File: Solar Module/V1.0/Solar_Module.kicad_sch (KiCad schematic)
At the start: 18 parts, among them J1 B2B-PH-K-S, U1 MT3608, U2 TP4057

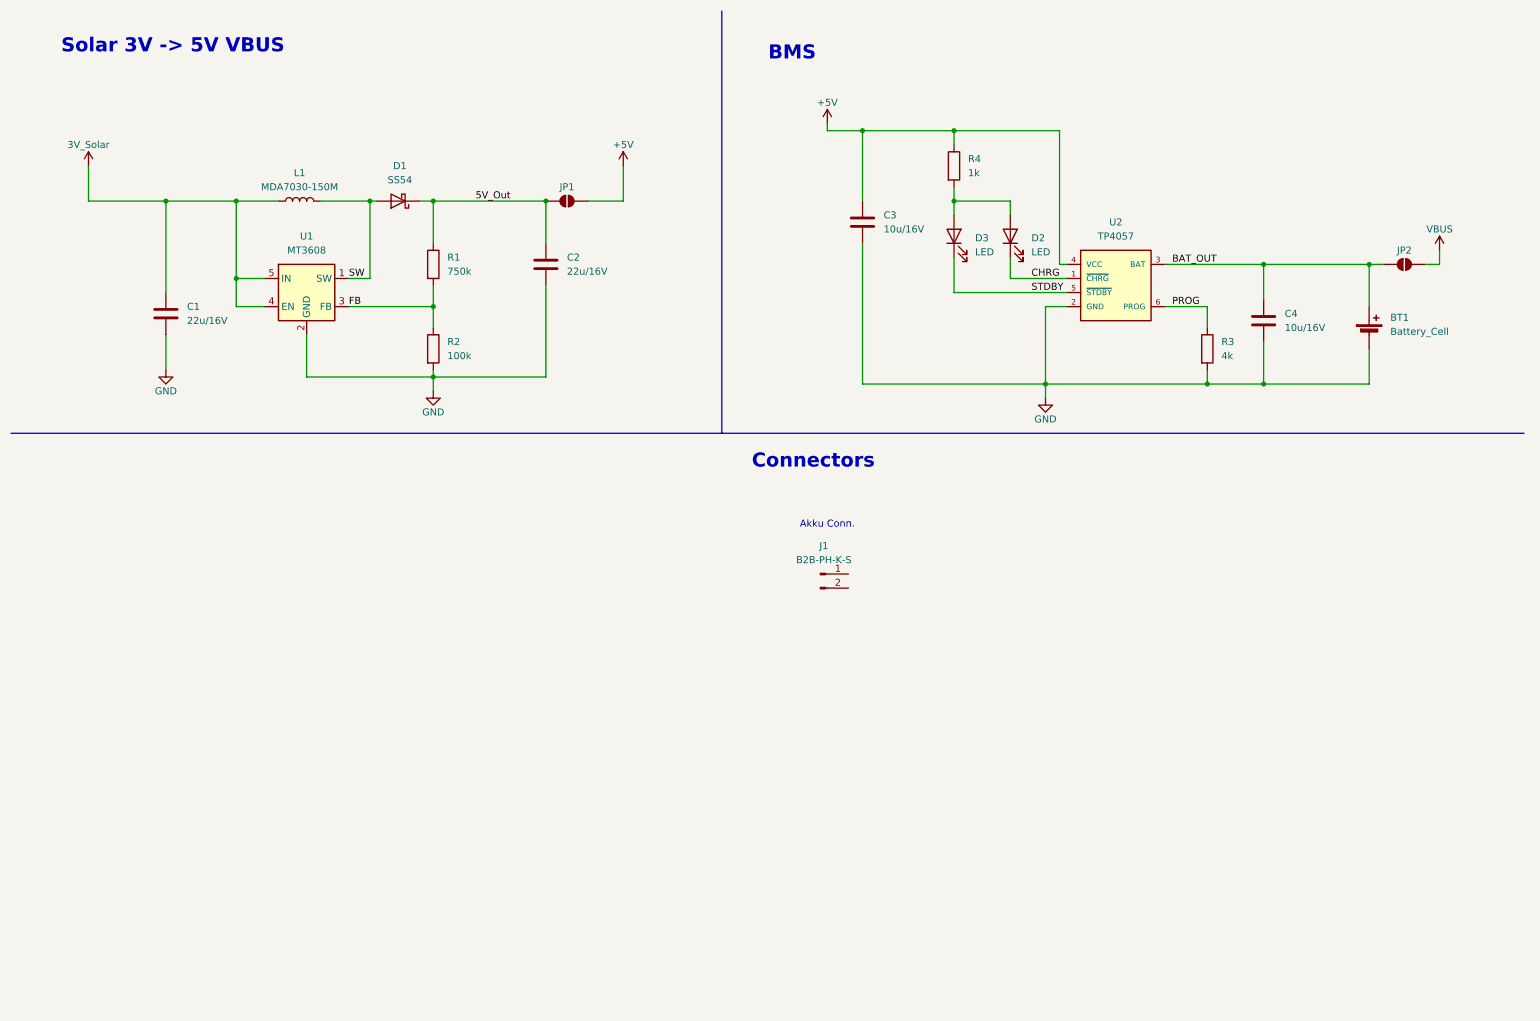
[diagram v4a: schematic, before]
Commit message: Added USB-C connector to schematic.
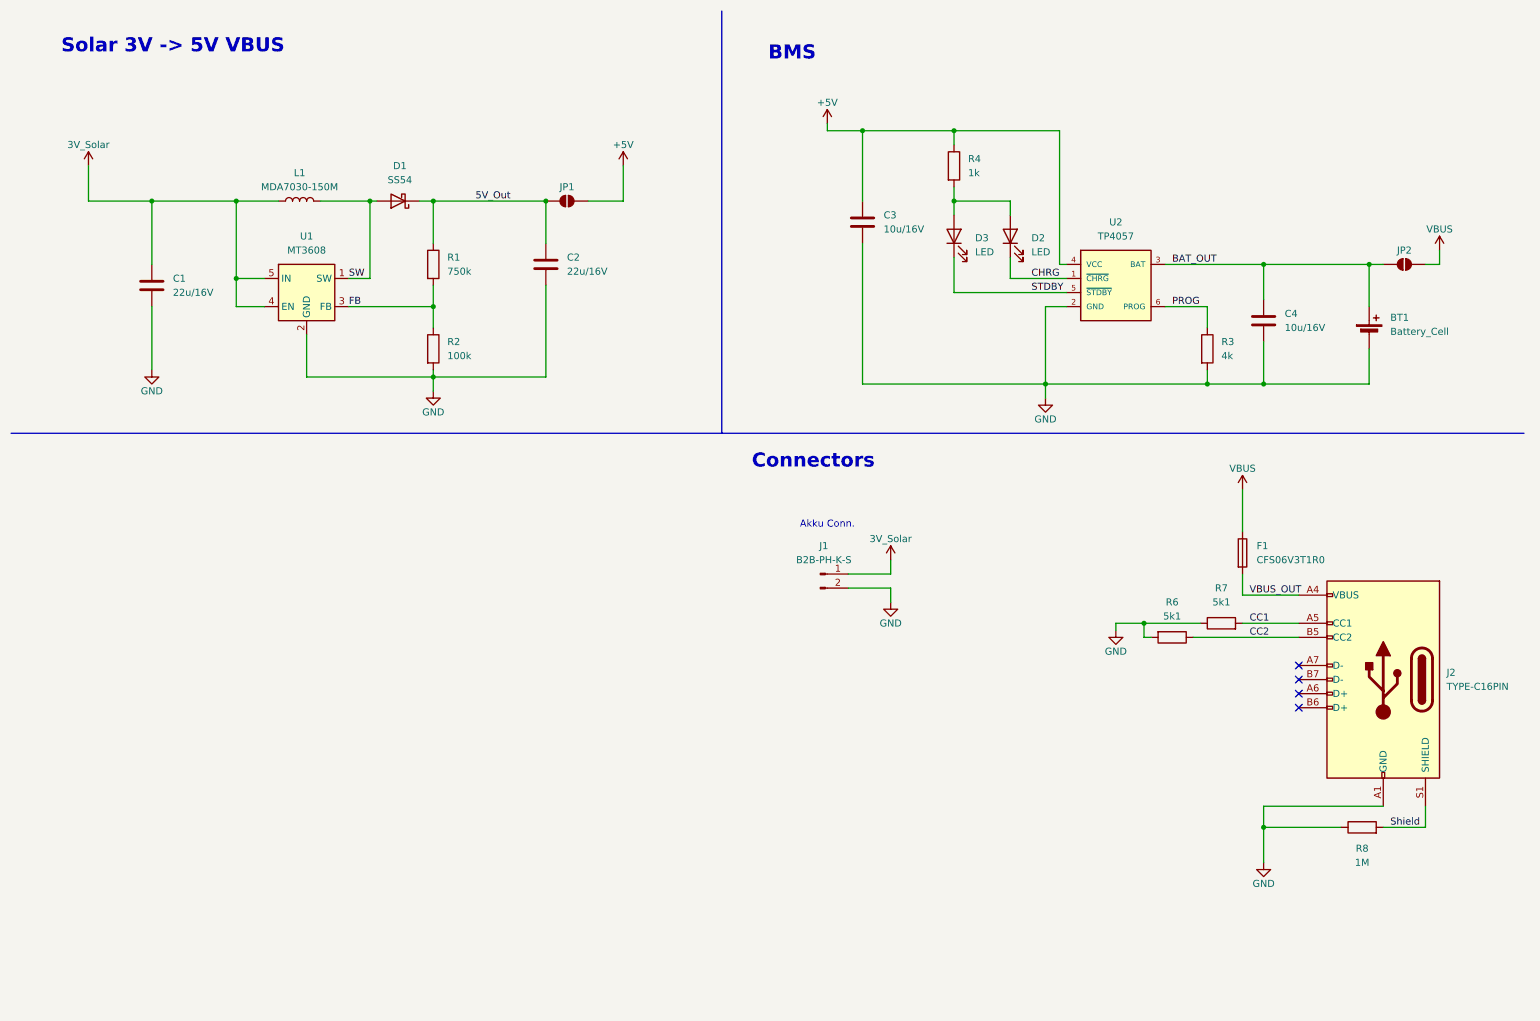
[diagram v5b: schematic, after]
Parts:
- added F1: CFS06V3T1R0, Fuse:Fuse_0603_1608Metric, symbol Device:Fuse
- added J2: TYPE-C16PIN, Connector_USB:USB_C_Receptacle_GCT_USB4105-xx-A_16P_TopMnt_Horizontal, symbol Connector:USB_C_Receptacle_USB2.0_14P
- added R6, R7: 5k1, Resistor_SMD:R_0603_1608Metric, symbol Device:R
- added R8: 1M, Resistor_SMD:R_0603_1608Metric, symbol Device:R
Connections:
- net 3V_Solar: now also J1.1 (Pin_1)
- net GND: now also J1.2 (Pin_2), J2.A1 (GND), J2.A12 (GND), J2.B1 (GND), J2.B12 (GND), R6.2, R7.1, R8.1
- net VBUS: now also F1.1
- new net CC1: J2.A5 (CC1), R7.2
- new net CC2: J2.B5 (CC2), R6.1
- new net Shield: J2.S1 (SHIELD), R8.2
- new net VBUS_OUT: F1.2, J2.A4 (VBUS), J2.A9 (VBUS), J2.B4 (VBUS), J2.B9 (VBUS)
- no-connect marks 0 -> 4
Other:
- moved on the sheet: C1

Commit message: Updated Schematics and nearly finished schematic.
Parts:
- removed BT1: Battery_Cell, symbol Device:Battery_Cell
- added J3: B2B-PH-K-S, Connector_JST:JST_EH_B2B-EH-A_1x02_P2.50mm_Vertical, symbol Connector:Conn_01x02_Pin
- C1, C2, C3, C4: footprint (none) -> Capacitor_SMD:C_0805_2012Metric
- D2, D3: footprint (none) -> LED_SMD:LED_0603_1608Metric
- JP1, JP2: footprint (none) -> Jumper:SolderJumper-2_P1.3mm_Open_TrianglePad1.0x1.5mm
- R1, R2, R3, R4: footprint (none) -> Resistor_SMD:R_0603_1608Metric
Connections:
- net BAT_OUT: now also J3.1 (Pin_1)
- net GND: now also J3.2 (Pin_2)
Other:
- note added: "Solar Panel"
- note added: "USB-C"
- moved on the sheet: F1, J1, J2, JP1, R6, R7, R8

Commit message: Rough design of DCDC.
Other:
- moved on the sheet: C2
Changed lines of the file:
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@@
 	(wire
 		(pts
-			(xy 107.95 62.23) (xy 107.95 78.74)
+			(xy 107.95 67.31) (xy 107.95 78.74)
 		)
 		(stroke
@@
 	(wire
 		(pts
-			(xy 107.95 46.99) (xy 107.95 54.61)
+			(xy 107.95 46.99) (xy 107.95 59.69)
 		)
 		(stroke
@@
 	(polyline
 		(pts
-			(xy 68.58 104.14) (xy 68.58 90.17)
+			(xy 68.58 104.14) (xy 68.58 88.9)
 		)
 		(stroke
@@
 	(symbol
 		(lib_id "Device:C")
-		(at 107.95 58.42 0)
+		(at 107.95 63.5 0)
 		(unit 1)
 		(exclude_from_sim no)
@@
 		(fields_autoplaced yes)
 		(property "Reference" "C2"
-			(at 111.76 57.1499 0)
+			(at 111.76 62.2299 0)
 			(effects
 				(font
@@
 		)
 		(property "Value" "22u/16V"
-			(at 111.76 59.6899 0)
+			(at 111.76 64.7699 0)
 			(effects
 				(font
@@
 		)
 		(property "Footprint" "Capacitor_SMD:C_0805_2012Metric"
-			(at 108.9152 62.23 0)
+			(at 108.9152 67.31 0)
 			(effects
 				(font
@@
 		)
 		(property "Datasheet" "~"
-			(at 107.95 58.42 0)
+			(at 107.95 63.5 0)
 			(effects
 				(font
@@
 		)
 		(property "Description" "Unpolarized capacitor"
-			(at 107.95 58.42 0)
-			(effects
-				(font
+			(at 107.95 63.5 0)
+			(effects
+				(font

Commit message: Added Production files.
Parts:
- D2: value LED -> KT-0603G
- D3: value LED -> KT-0603R
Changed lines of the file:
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@@
 			)
 		)
-		(property "Value" "LED"
+		(property "Value" "KT-0603G"
 			(at 195.58 56.1974 90)
 			(effects
@@
 				)
 				(justify right)
+				(hide yes)
 			)
 		)
@@
 			)
 		)
-		(property "Value" "LED"
+		(property "Value" "KT-0603R"
 			(at 185.42 56.1974 90)
 			(effects
@@
 				)
 				(justify right)
-			)
-		)
+				(hide yes)
+			)
+		)
